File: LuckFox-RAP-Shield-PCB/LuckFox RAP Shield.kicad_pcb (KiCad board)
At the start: 2 copper layers, 45 x 62.6 mm, 8 parts, among them J1 LuckFox_Pico_Mini_Connector, J2 External_5V_Input_from_Buck_M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, U2 W5500_Ethernet_Module_DNP_on_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

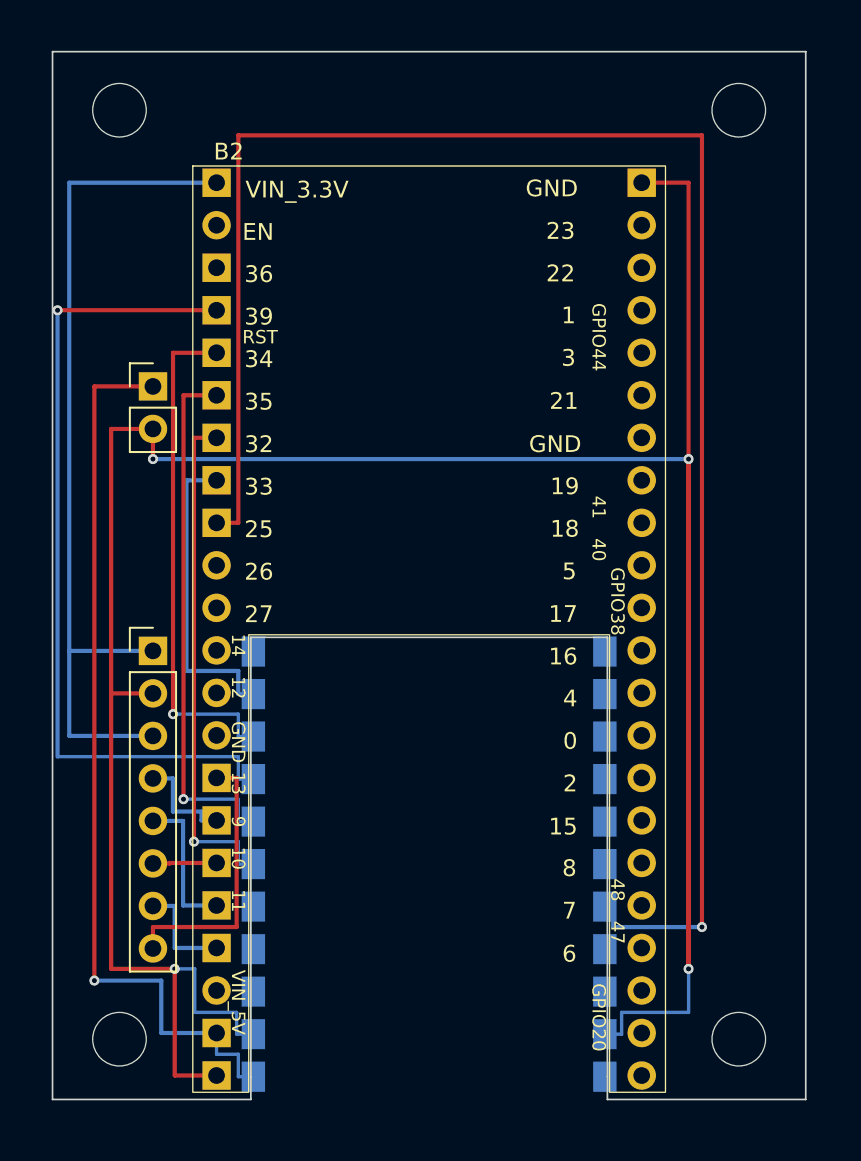
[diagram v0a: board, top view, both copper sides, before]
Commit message: Reroute LuckFox SPI net swap onto real copper, fix GND edge routing, flip headers bottom-only
Routes the 8 swapped LF/ETH SPI nets (J1/B2/U2 pads renamed in a prior
commit but left as ratsnest) as real 0.2mm traces. Reworks the GND
connection from J1's two GND pads to the board's zone fill -- earlier
routing detoured all the way to the board's far corners and briefly ran
copper over the open LuckFox nesting-slot cutout with no substrate
underneath; now a short, direct stub into the nearby fill next to B2's own
GND pad. Also flips ESP32 (B2), the Ethernet header (U2), and the power
header (J2) to bottom-only solder-mask exposure, matching how they're
actually soldered.

Co-Authored-By: Claude Sonnet 5 <noreply@anthropic.com>
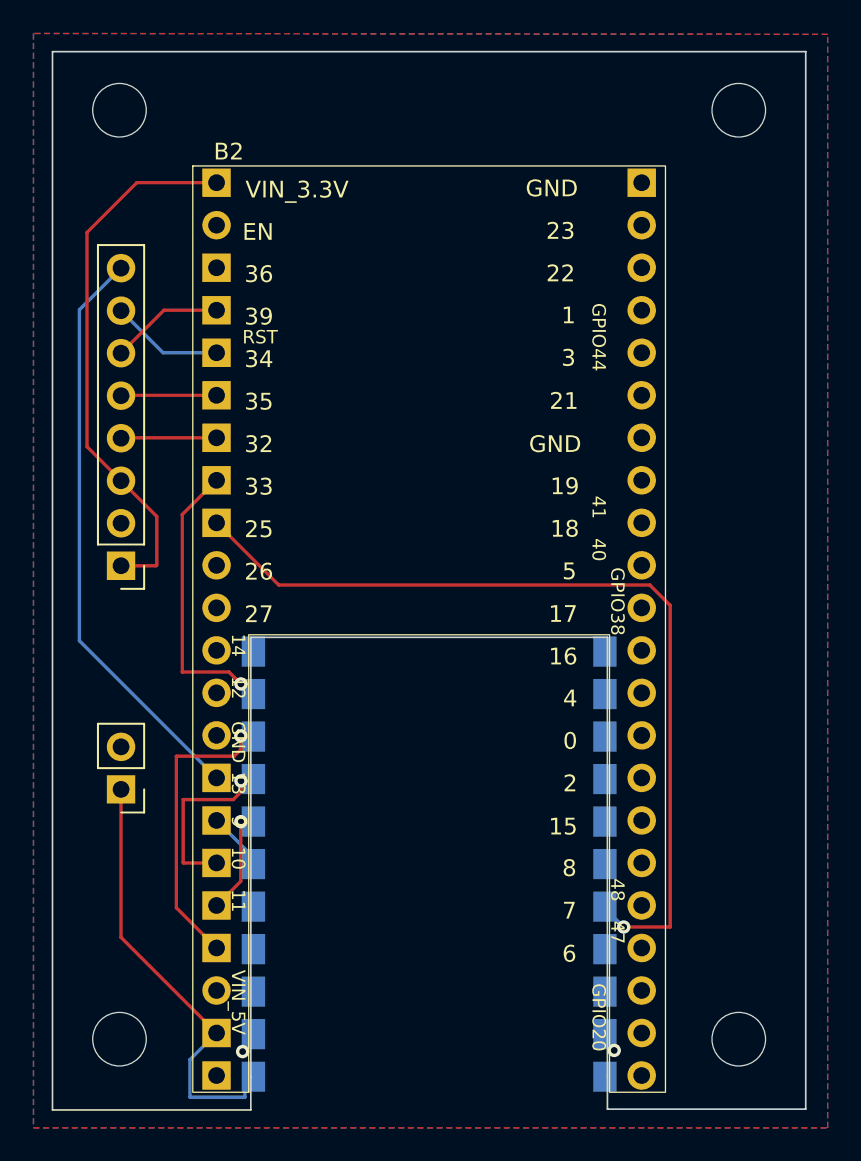
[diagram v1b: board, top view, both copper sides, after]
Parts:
- moved J2 24.2 mm to (117.1, 119.1), turned to 180 degrees
- moved U2 5.43 mm to (117.1, 105.7), turned to 180 degrees
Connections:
- B2 pad 10: Net-(B2-GPIO10_CS_ETH) -> Net-(B2-GPIO10_CS_LF)
- B2 pad 11: Net-(B2-GPIO11_MOSI_ETH) -> Net-(B2-GPIO11_MOSI_LF)
- B2 pad 12: Net-(B2-GPIO12_SCK_ETH) -> Net-(B2-GPIO12_SCK_LF)
- B2 pad 13: Net-(B2-GPIO13_MISO_ETH) -> Net-(B2-GPIO13_MISO_LF)
- B2 pad 5: Net-(B2-GPIO4_MOSI_LF) -> Net-(B2-GPIO4_MOSI_ETH)
- B2 pad 6: Net-(B2-GPIO5_MISO_LF) -> Net-(B2-GPIO5_MISO_ETH)
- B2 pad 7: Net-(B2-GPIO6_SCK_LF) -> Net-(B2-GPIO6_SCK_ETH)
- B2 pad 8: Net-(B2-GPIO7_CS_LF) -> Net-(B2-GPIO7_CS_ETH)
- J1 pad 6: Net-(B2-GPIO7_CS_LF) -> Net-(B2-GPIO10_CS_LF)
- J1 pad 7: Net-(B2-GPIO6_SCK_LF) -> Net-(B2-GPIO12_SCK_LF)
- J1 pad 8: Net-(B2-GPIO4_MOSI_LF) -> Net-(B2-GPIO11_MOSI_LF)
- J1 pad 9: Net-(B2-GPIO5_MISO_LF) -> Net-(B2-GPIO13_MISO_LF)
- U2 pad 4: Net-(B2-GPIO10_CS_ETH) -> Net-(B2-GPIO7_CS_ETH)
- U2 pad 5: Net-(B2-GPIO12_SCK_ETH) -> Net-(B2-GPIO6_SCK_ETH)
- U2 pad 6: Net-(B2-GPIO11_MOSI_ETH) -> Net-(B2-GPIO4_MOSI_ETH)
- U2 pad 7: Net-(B2-GPIO13_MISO_ETH) -> Net-(B2-GPIO5_MISO_ETH)
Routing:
- net GND: track 180.7 -> 1.20 mm, vias 4 -> 2
- net Net-(B2-GPIO16_SLAVE_RDY_OUT): track 106.1 -> 52.7 mm
- net Net-(B2-GPIO4_MOSI_LF): track 48.8 -> 0.00 mm, vias 1 -> 0
- net Net-(B2-GPIO6_SCK_LF): track 31.2 -> 0.00 mm, vias 1 -> 0
- net Net-(B2-GPIO7_CS_LF): track 30.0 -> 0.00 mm, vias 1 -> 0
- net Net-(B2-GPIO5_MISO_LF): track 29.9 -> 0.00 mm, vias 1 -> 0
- net +5V_RAIL: track 53.8 -> 26.9 mm, vias 1 -> 0
- net +3V3_RAIL: track 51.8 -> 32.7 mm
- net Net-(B2-GPIO9_INT_ETH): track 16.4 -> 34.9 mm
- net Net-(B2-GPIO13_MISO_LF): track 0.00 -> 17.9 mm, vias 0 -> 1
- net Net-(B2-GPIO11_MOSI_LF): track 0.00 -> 10.7 mm, vias 0 -> 1
- net Net-(B2-GPIO12_SCK_ETH): track 8.85 -> 0.00 mm
- net Net-(B2-GPIO4_MOSI_ETH): track 0.00 -> 6.77 mm
- net Net-(B2-GPIO5_MISO_ETH): track 0.00 -> 6.75 mm
- net Net-(B2-GPIO13_MISO_ETH): track 6.31 -> 0.00 mm
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- added copper zone on B.Cu, net GND
- added copper zone on F.Cu, net GND
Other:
- board size 45 x 62.6 mm -> 45 x 63.2 mm
